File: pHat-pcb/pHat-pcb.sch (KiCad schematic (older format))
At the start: 13 parts, among them J1 Conn_02x20_Odd_Even, J2 Conn_01x24_Male, J3 Conn_Active_High, J4 Conn_Bat, J5 Conn_I2C, J8 Conn_Active_Low, SW1 SW_Push, U1 TPS61023_Breakout, U2 74HC74, U3 DS3231M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

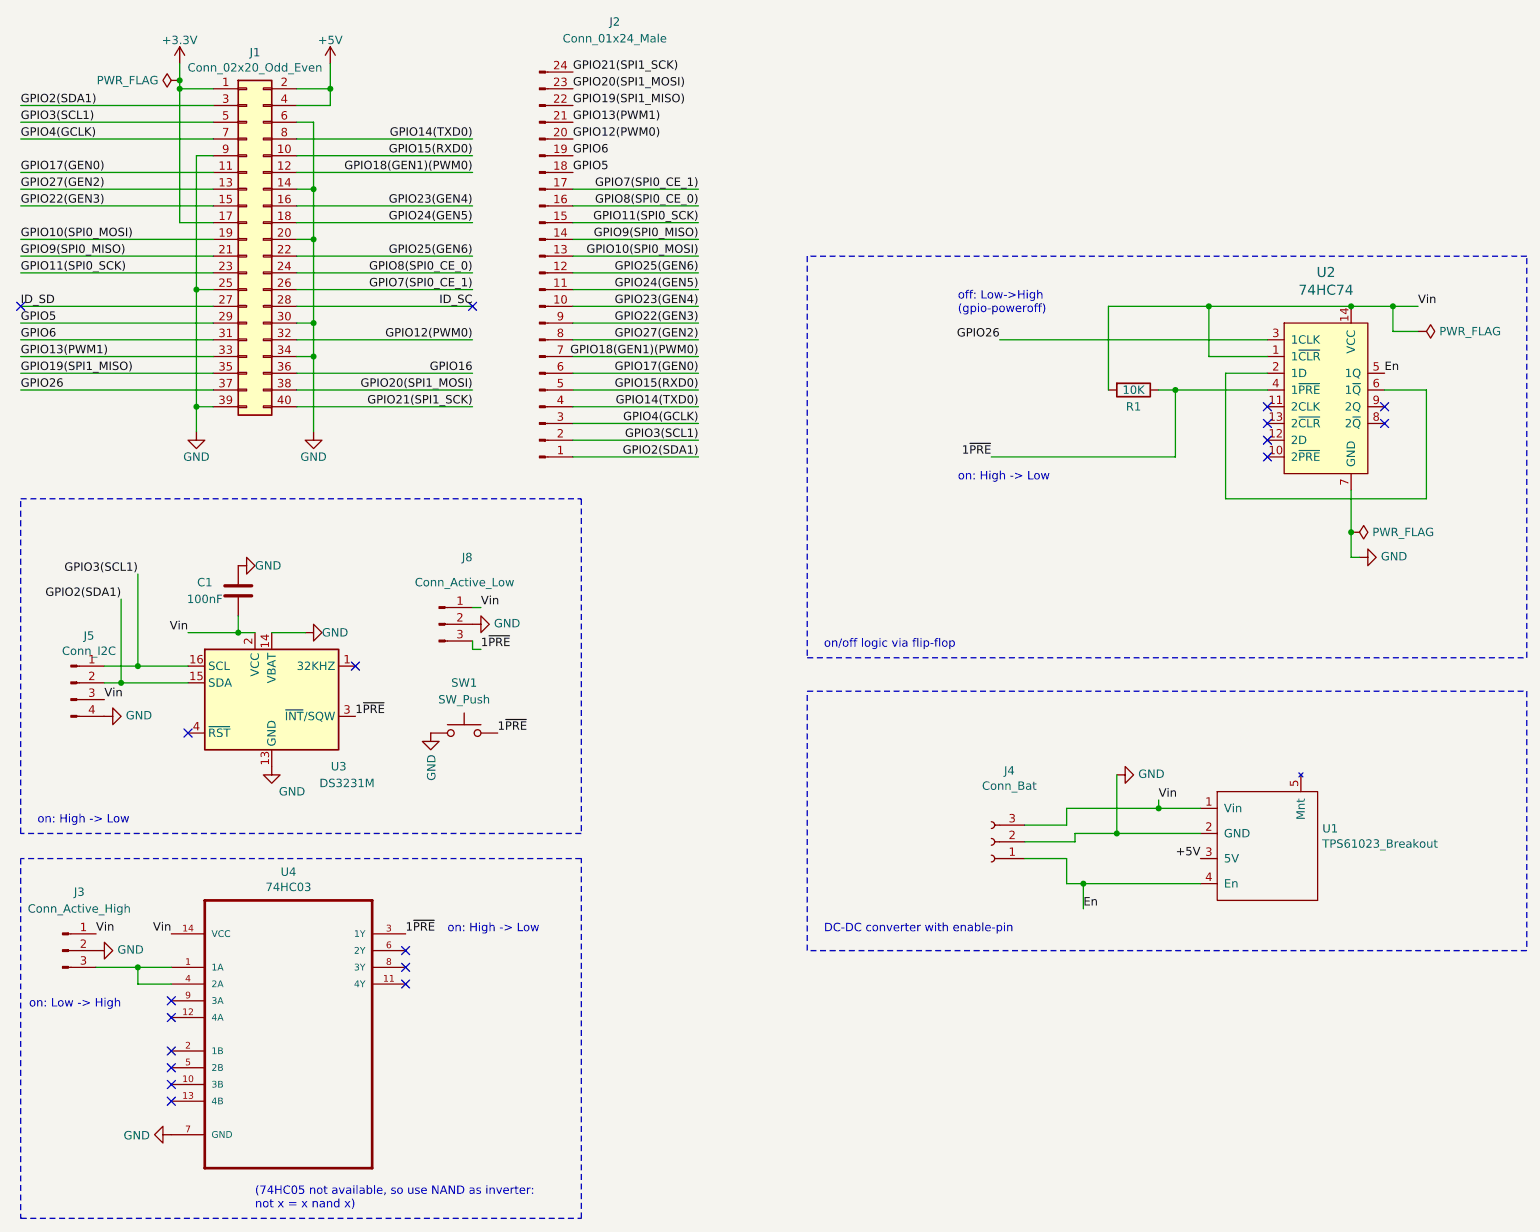
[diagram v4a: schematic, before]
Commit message: Rev3: added power-control IC and LED
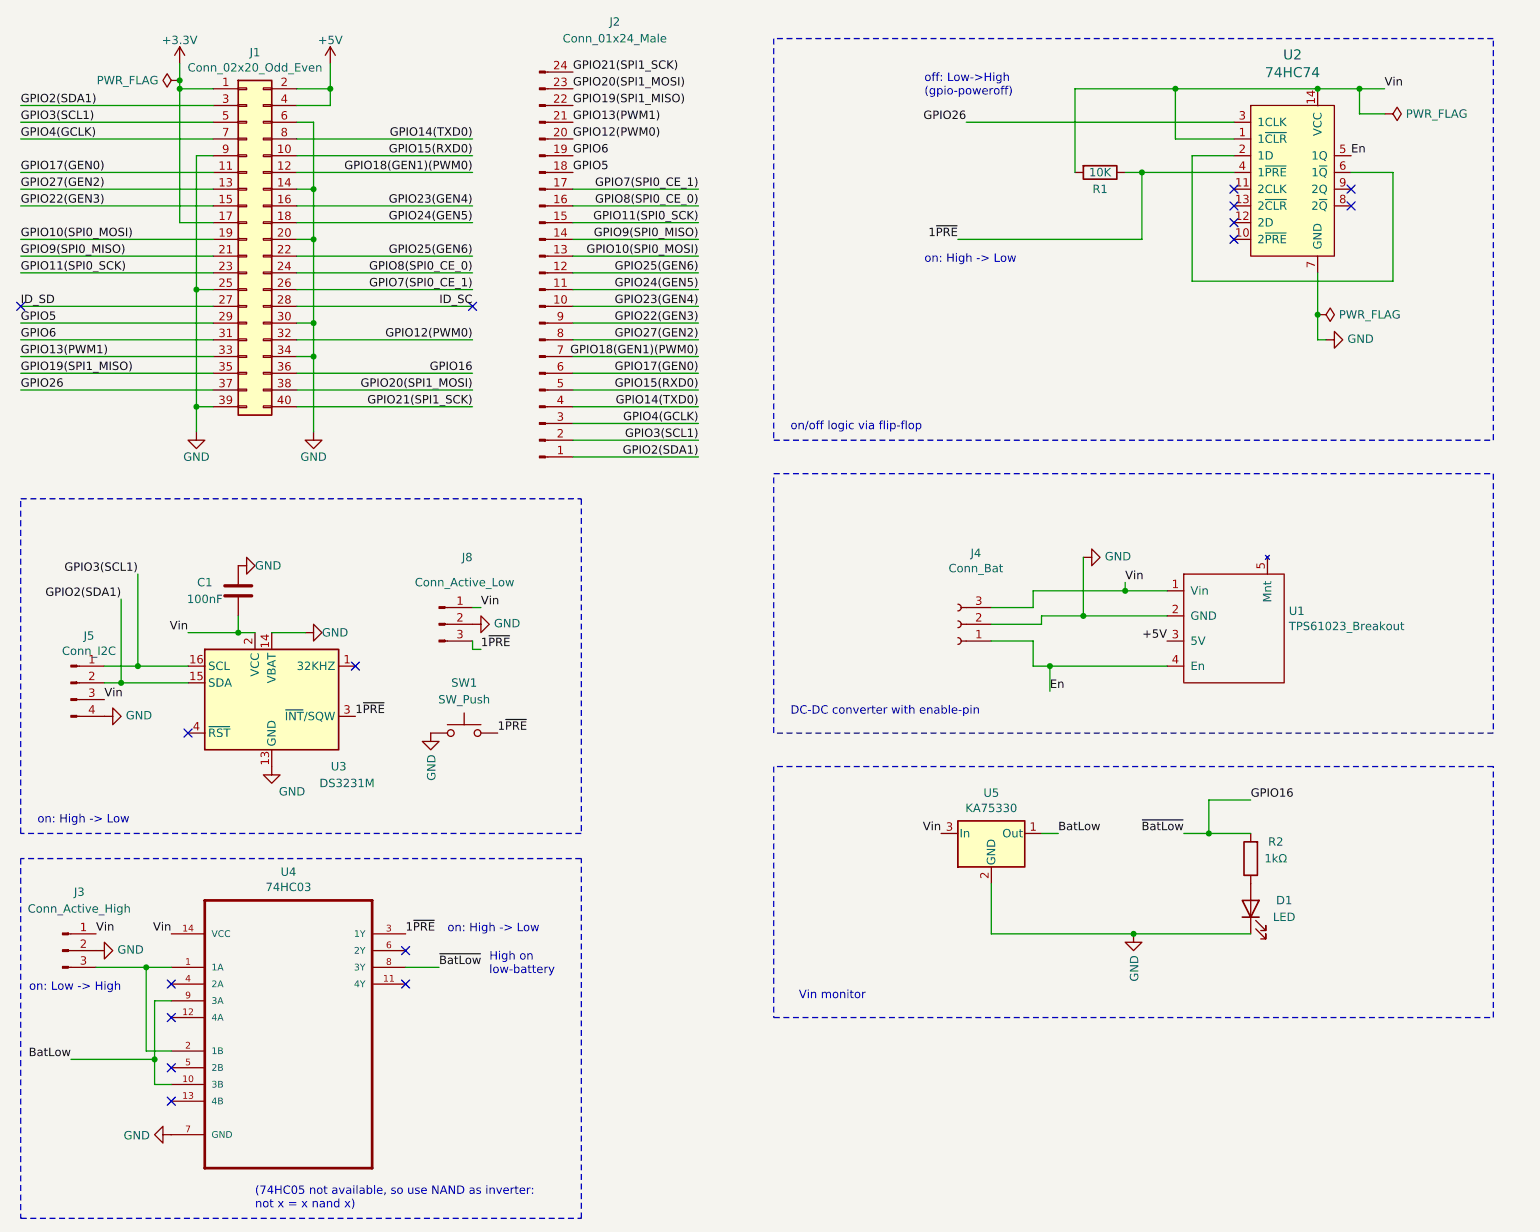
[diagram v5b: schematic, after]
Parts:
- added D1: LED, LED_SMD:LED_1206_3216Metric_Pad1.42x1.75mm_HandSolder, symbol Device:LED
- added R2: 1kΩ, Resistor_SMD:R_1206_3216Metric_Pad1.30x1.75mm_HandSolder, symbol Device:R
- added U5: KA75330, Package_TO_SOT_THT:TO-92_Inline_Wide, symbol User:KA75330
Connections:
- net GND: now also D1.1 (K), U5.2 (GND)
- net GPIO16: now also U4.8 (3Y), R2.2
- net Vin: now also U5.3 (In)
- net at J3.3 (Pin_3), U4.1 (1A): now also U4.2 (1B); no longer U4.4 (2A)
- net BatLow: now reaches U4.10 (3B)
- net BatLow: now also U4.9 (3A), U5.1 (Out)
- new net: D1.2 (A), R2.1
- no-connect marks 19 -> 16
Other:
- note added: "High on\nlow-battery"
- note added: "Vin monitor"
- moved on the sheet: J4, R1, U1, U2

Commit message: Rev4: added interrupt-pin for external I2C-connector
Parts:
- J5: footprint Connector_PinHeader_2.54mm:PinHeader_1x04_P2.54mm_Vertical -> Connector_PinHeader_2.54mm:PinHeader_1x05_P2.54mm_Vertical; symbol Connector:Conn_01x04_Male -> Connector:Conn_01x05_Male
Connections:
- net 1~PRE: now also J5.5 (Pin_5)
- net GND: now also J5.1 (Pin_1); no longer J5.4 (Pin_4)
- net GPIO2(SDA1): now also J5.3 (Pin_3); no longer J5.2 (Pin_2)
- net GPIO3(SCL1): now also J5.4 (Pin_4); no longer J5.1 (Pin_1)
- net Vin: now also J5.2 (Pin_2); no longer J5.3 (Pin_3)
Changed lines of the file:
@@
 Sheet 1 1
 Title "Pi Battery Management pHat"
-Date "2020-10-19"
-Rev "3"
+Date "2020-10-21"
+Rev "4"
 Comp "Bernhard Bablok"
 Comment1 "https://github.com/bablokb/pcb-pi-batman"
@@
 $EndComp
 $Comp
-L Connector:Conn_01x04_Male J5
+L Connector:Conn_01x05_Male J5
 U 1 1 5F760C28
 P 950 4500
-F 0 "J5" H 1058 4781 50  0000 C CNN
-F 1 "Conn_I2C" H 1058 4690 50  0000 C CNN
-F 2 "Connector_PinHeader_2.54mm:PinHeader_1x04_P2.54mm_Vertical" H 950 4500 50  0001 C CNN
+F 0 "J5" H 1100 4050 50  0000 C CNN
+F 1 "Conn_I2C" H 1100 4150 50  0000 C CNN
+F 2 "Connector_PinHeader_2.54mm:PinHeader_1x05_P2.54mm_Vertical" H 950 4500 50  0001 C CNN
 F 3 "~" H 950 4500 50  0001 C CNN
 	1    950  4500
-	1    0    0    -1
+	1    0    0    1
 $EndComp
 $Comp
@@
 	0    -1   -1   0
 $EndComp
-Wire Wire Line
-	1150 4400 1350 4400
-Wire Wire Line
-	1150 4500 1250 4500
 $Comp
 L power:PWR_FLAG #FLG0101
@@
 Wire Wire Line
 	6700 3950 7250 3950
-Text Label 1250 4000 2    50   ~ 0
+Text Label 1400 4000 2    50   ~ 0
 GPIO2(SDA1)
-Text Label 1350 3850 2    50   ~ 0
+Text Label 1500 3850 2    50   ~ 0
 GPIO3(SCL1)
 Wire Wire Line
-	1350 3850 1350 4400
-Connection ~ 1350 4400
-Wire Wire Line
-	1350 4400 1650 4400
-Wire Wire Line
-	1250 4000 1250 4500
-Connection ~ 1250 4500
-Wire Wire Line
-	1250 4500 1650 4500
+	1500 3850 1500 4400
+Wire Wire Line
+	1400 4000 1400 4500
 $Comp
 L power:GND #PWR0109
@@
 Text Notes 5300 6400 0    50   ~ 0
 Vin monitor
+Text Label 1150 4300 0    50   ~ 0
+1~PRE
+Connection ~ 1400 4500
+Wire Wire Line
+	1400 4500 1650 4500
+Wire Wire Line
+	1150 4500 1400 4500
+Connection ~ 1500 4400
+Wire Wire Line
+	1500 4400 1650 4400
+Wire Wire Line
+	1150 4400 1500 4400
 $EndSCHEMATC

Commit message: replaced 74HC03 (nand) with 74HC05 (inverter)
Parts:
- U4: value 74HC03 -> SN74HC05N; symbol User:74HC03 -> User:SN74HC05N
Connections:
- net 1~PRE: now also U4.2 (1Y); no longer U4.3 (1Y)
- net BatLow: no longer U4.10 (3B)
- net GND: now also U4.11 (5A), U4.13 (6A), U4.3 (2A), U4.5 (3A)
- net GPIO16: now also U4.10 (5Y); no longer U4.8 (3Y)
- net at J3.3 (Pin_3), U4.1 (1A): no longer U4.2 (1B)
- no-connect marks 16 -> 14
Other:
- note removed: "(74HC05 not available, so use NAND as inverter:\nnot x = x nand x)"
- moved on the sheet: J3
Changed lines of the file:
@@
 Sheet 1 1
 Title "Pi Battery Management pHat"
-Date "2020-10-21"
-Rev "4"
+Date "2020-10-23"
+Rev "5"
 Comp "Bernhard Bablok"
 Comment1 "https://github.com/bablokb/pcb-pi-batman"
@@
 L Connector:Conn_01x03_Male J3
 U 1 1 5F761E95
-P 900 6100
-F 0 "J3" H 1000 6450 50  0000 C CNN
-F 1 "Conn_Active_High" H 1000 6350 50  0000 C CNN
-F 2 "Connector_PinHeader_2.54mm:PinHeader_1x03_P2.54mm_Vertical" H 900 6100 50  0001 C CNN
-F 3 "~" H 900 6100 50  0001 C CNN
-	1    900  6100
+P 1300 6100
+F 0 "J3" H 1400 6450 50  0000 C CNN
+F 1 "Conn_Active_High" H 1400 6350 50  0000 C CNN
+F 2 "Connector_PinHeader_2.54mm:PinHeader_1x03_P2.54mm_Vertical" H 1300 6100 50  0001 C CNN
+F 3 "~" H 1300 6100 50  0001 C CNN
+	1    1300 6100
 	1    0    0    -1
 $EndComp
@@
 L power:GND #PWR0107
 U 1 1 5F7A5C5F
-P 1100 6100
-F 0 "#PWR0107" H 1100 5850 50  0001 C CNN
-F 1 "GND" V 1105 5972 50  0000 R CNN
-F 2 "" H 1100 6100 50  0001 C CNN
-F 3 "" H 1100 6100 50  0001 C CNN
-	1    1100 6100
+P 1500 6100
+F 0 "#PWR0107" H 1500 5850 50  0001 C CNN
+F 1 "GND" V 1505 5972 50  0000 R CNN
+F 2 "" H 1500 6100 50  0001 C CNN
+F 3 "" H 1500 6100 50  0001 C CNN
+	1    1500 6100
 	0    -1   -1   0
 $EndComp
-Text Label 1100 6000 0    50   ~ 0
+Text Label 1500 6000 0    50   ~ 0
 Vin
 Wire Notes Line
@@
 Wire Wire Line
 	8650 950  8400 950
-Wire Wire Line
-	1100 6200 1400 6200
-Text Label 2950 6000 0    50   ~ 0
+Text Label 2550 6200 0    50   ~ 0
 1~PRE
-NoConn ~ 1550 6500
-NoConn ~ 1550 6800
-NoConn ~ 1550 7000
-Text Label 1550 6000 2    50   ~ 0
+Text Label 2250 5900 2    50   ~ 0
 Vin
 $Comp
 L power:GND #PWR0108
 U 1 1 5F7888FE
-P 1550 7200
-F 0 "#PWR0108" H 1550 6950 50  0001 C CNN
-F 1 "GND" V 1555 7072 50  0000 R CNN
-F 2 "" H 1550 7200 50  0001 C CNN
-F 3 "" H 1550 7200 50  0001 C CNN
-	1    1550 7200
-	0    1    1    0
+P 2250 7150
+F 0 "#PWR0108" H 2250 6900 50  0001 C CNN
+F 1 "GND" V 2255 7022 50  0000 R CNN
+F 2 "" H 2250 7150 50  0001 C CNN
+F 3 "" H 2250 7150 50  0001 C CNN
+	1    2250 7150
+	1    0    0    -1
 $EndComp
 Wire Wire Line
@@
 	7000 4100 7500 4100
 $Comp
-L User:74HC03 U4
+L User:SN74HC05N U4
 U 1 1 5F7922BA
 P 2250 6500
 F 0 "U4" H 2250 7370 50  0000 C CNN
-F 1 "74HC03" H 2250 7279 50  0000 C CNN
+F 1 "SN74HC05N" H 2250 7279 50  0000 C CNN
 F 2 "user:SO-14_3.9x8.65mm_P1.27mm_HandSolder" H 2250 6500 50  0001 L BNN
 F 3 "NXP" H 2250 6500 50  0001 L BNN
@@
 	1    0    0    -1
 $EndComp
-Connection ~ 1400 6200
-Wire Wire Line
-	1400 6200 1550 6200
-NoConn ~ 2950 6100
-NoConn ~ 2950 6300
 Wire Notes Line
 	4000 5550 650  5550
@@
 Wire Notes Line
 	4000 7700 4000 5550
-Text Notes 700  6350 0    50   ~ 0
+Text Notes 1100 6350 0    50   ~ 0
 on: Low -> High
 Wire Notes Line
@@
 Text Notes 5250 4700 0    50   ~ 0
 DC-DC converter with enable-pin
-Text Notes 2050 7650 0    50   ~ 0
-(74HC05 not available, so use NAND as inverter:\nnot x = x nand x)
 Wire Wire Line
 	6250 1850 7350 1850
@@
 Text Notes 6050 2000 0    50   ~ 0
 on: High -> Low
-Text Notes 3200 6000 0    50   ~ 0
+Text Notes 2800 6200 0    50   ~ 0
 on: High -> Low
 Text Label 7250 3900 0    50   ~ 0
@@
 	6850 5400 6750 5400
 Wire Wire Line
-	1400 6700 1550 6700
-Wire Wire Line
-	1400 6200 1400 6700
-NoConn ~ 1550 6300
-Wire Wire Line
-	950  6750 1450 6750
-Wire Wire Line
-	1450 6750 1450 6400
-Wire Wire Line
-	1450 6400 1550 6400
-Wire Wire Line
-	1450 6750 1450 6900
-Wire Wire Line
-	1450 6900 1550 6900
-Connection ~ 1450 6750
-Text Notes 3450 6250 0    50   ~ 0
+	1450 6500 1950 6500
+Text Notes 3050 6650 0    50   ~ 0
 High on\nlow-battery
-Text Label 3150 6200 0    50   ~ 0
+Text Label 2750 6600 0    50   ~ 0
 ~BatLow
-Text Label 950  6750 2    50   ~ 0
+Text Label 1450 6500 2    50   ~ 0
 BatLow
 Wire Wire Line
-	2950 6200 3150 6200
+	2550 6600 2750 6600
 Text Label 7600 5400 2    50   ~ 0
 ~BatLow
@@
 Wire Wire Line
 	1150 4400 1500 4400
+Wire Wire Line
+	1500 6200 1950 6200
+NoConn ~ 2550 6300
+NoConn ~ 2550 6400
+NoConn ~ 2550 6500
+NoConn ~ 2550 6700
+Wire Wire Line
+	1950 6300 1850 6300
+Wire Wire Line
+	1850 6300 1850 6400
+Wire Wire Line
+	1850 7050 2250 7050
+Wire Wire Line
+	2250 7050 2250 7000
+Wire Wire Line
+	2250 7050 2250 7150
+Connection ~ 2250 7050
+Wire Wire Line
+	1950 6400 1850 6400
+Connection ~ 1850 6400
+Wire Wire Line
+	1950 6700 1850 6700
+Connection ~ 1850 6700
+Wire Wire Line
+	1850 6700 1850 7050
+Wire Wire Line
+	1850 6400 1850 6600
+Wire Wire Line
+	1950 6600 1850 6600
+Connection ~ 1850 6600
+Wire Wire Line
+	1850 6600 1850 6700
 $EndSCHEMATC

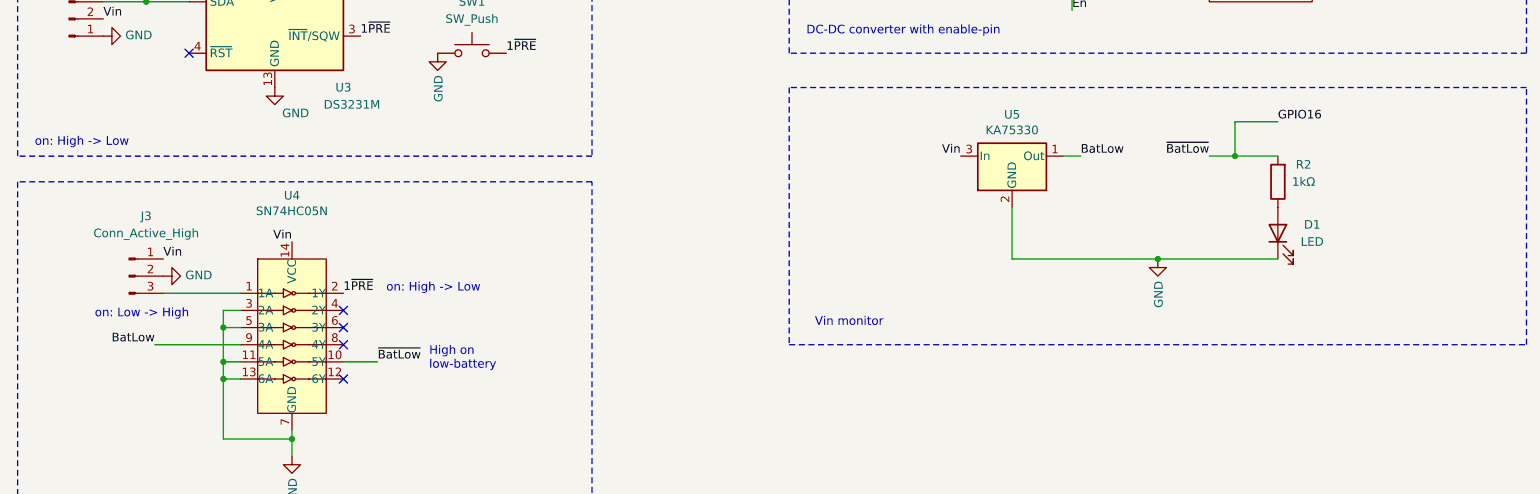
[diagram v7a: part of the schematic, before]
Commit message: Rev5: drive LED from GPIO06
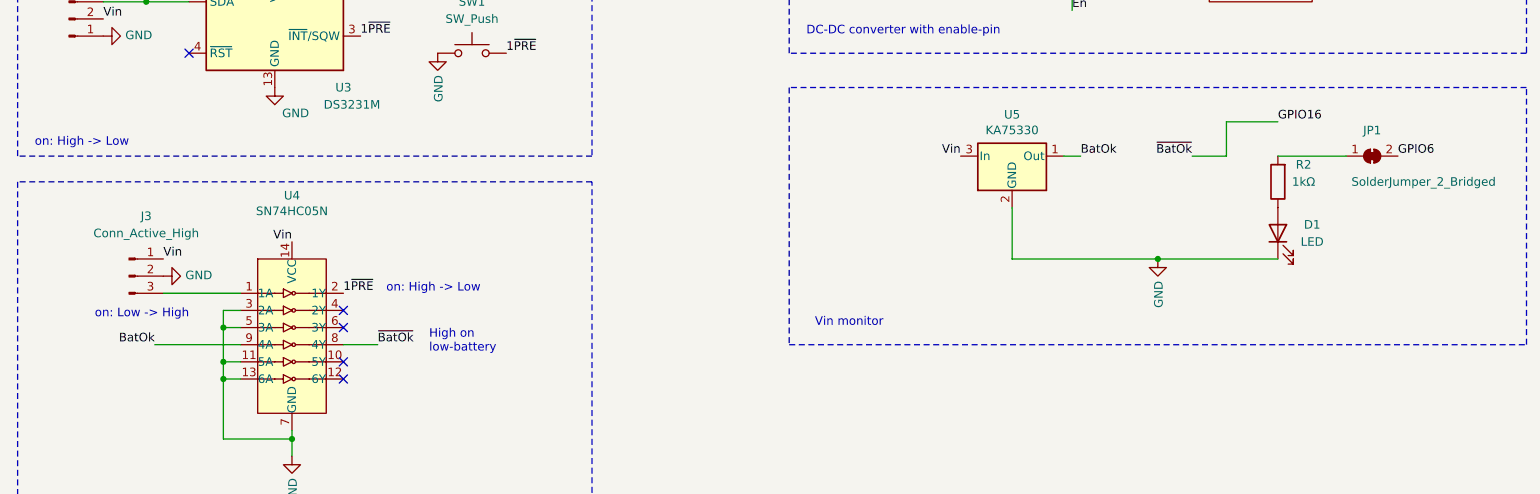
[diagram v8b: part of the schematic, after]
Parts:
- added JP1: SolderJumper_2_Bridged, Jumper:SolderJumper-2_P1.3mm_Bridged_Pad1.0x1.5mm, symbol Jumper:SolderJumper_2_Bridged
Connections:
- net GPIO16: now also U4.8 (4Y); no longer R2.2, U4.10 (5Y)
- net GPIO6: now also JP1.2 (B)
- net BatLow renamed BatOk
- new net: JP1.1 (A), R2.2
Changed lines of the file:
@@
 	6450 5700 6450 6000
 Text Label 6850 5400 0    50   ~ 0
-BatLow
+BatOk
 Wire Wire Line
 	6850 5400 6750 5400
 Wire Wire Line
 	1450 6500 1950 6500
-Text Notes 3050 6650 0    50   ~ 0
+Text Notes 3050 6550 0    50   ~ 0
 High on\nlow-battery
-Text Label 2750 6600 0    50   ~ 0
-~BatLow
+Text Label 2750 6500 0    50   ~ 0
+~BatOk
 Text Label 1450 6500 2    50   ~ 0
-BatLow
+BatOk
 Wire Wire Line
-	2550 6600 2750 6600
-Text Label 7600 5400 2    50   ~ 0
-~BatLow
-Wire Wire Line
-	7600 5400 7750 5400
+	2550 6500 2750 6500
+Text Label 7500 5400 2    50   ~ 0
+~BatOk
 Text Label 8000 5200 0    50   ~ 0
 GPIO16
-Wire Wire Line
-	7750 5400 7750 5200
-Wire Wire Line
-	7750 5200 8000 5200
-Connection ~ 7750 5400
-Wire Wire Line
-	7750 5400 8000 5400
 Connection ~ 7300 6000
 Wire Wire Line
@@
 NoConn ~ 2550 6300
 NoConn ~ 2550 6400
-NoConn ~ 2550 6500
 NoConn ~ 2550 6700
 Wire Wire Line
@@
 Wire Wire Line
 	1850 6600 1850 6700
+$Comp
+L Jumper:SolderJumper_2_Bridged JP1
+U 1 1 5F9ABDE0
+P 8550 5400
+F 0 "JP1" H 8550 5550 50  0000 C CNN
+F 1 "SolderJumper_2_Bridged" H 8850 5250 50  0000 C CNN
+F 2 "Jumper:SolderJumper-2_P1.3mm_Bridged_Pad1.0x1.5mm" H 8550 5400 50  0001 C CNN
+F 3 "~" H 8550 5400 50  0001 C CNN
+	1    8550 5400
+	1    0    0    -1
+$EndComp
+Wire Wire Line
+	8000 5400 8400 5400
+Text Label 8700 5400 0    50   ~ 0
+GPIO6
+Wire Wire Line
+	7500 5400 7700 5400
+Wire Wire Line
+	7700 5400 7700 5200
+Wire Wire Line
+	7700 5200 8000 5200
+NoConn ~ 2550 6600
 $EndSCHEMATC
